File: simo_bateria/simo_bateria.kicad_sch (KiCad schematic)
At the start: 7 parts, among them J1 conector_bateria, J2 conector_bateria, U1 conversor_dc_1_1

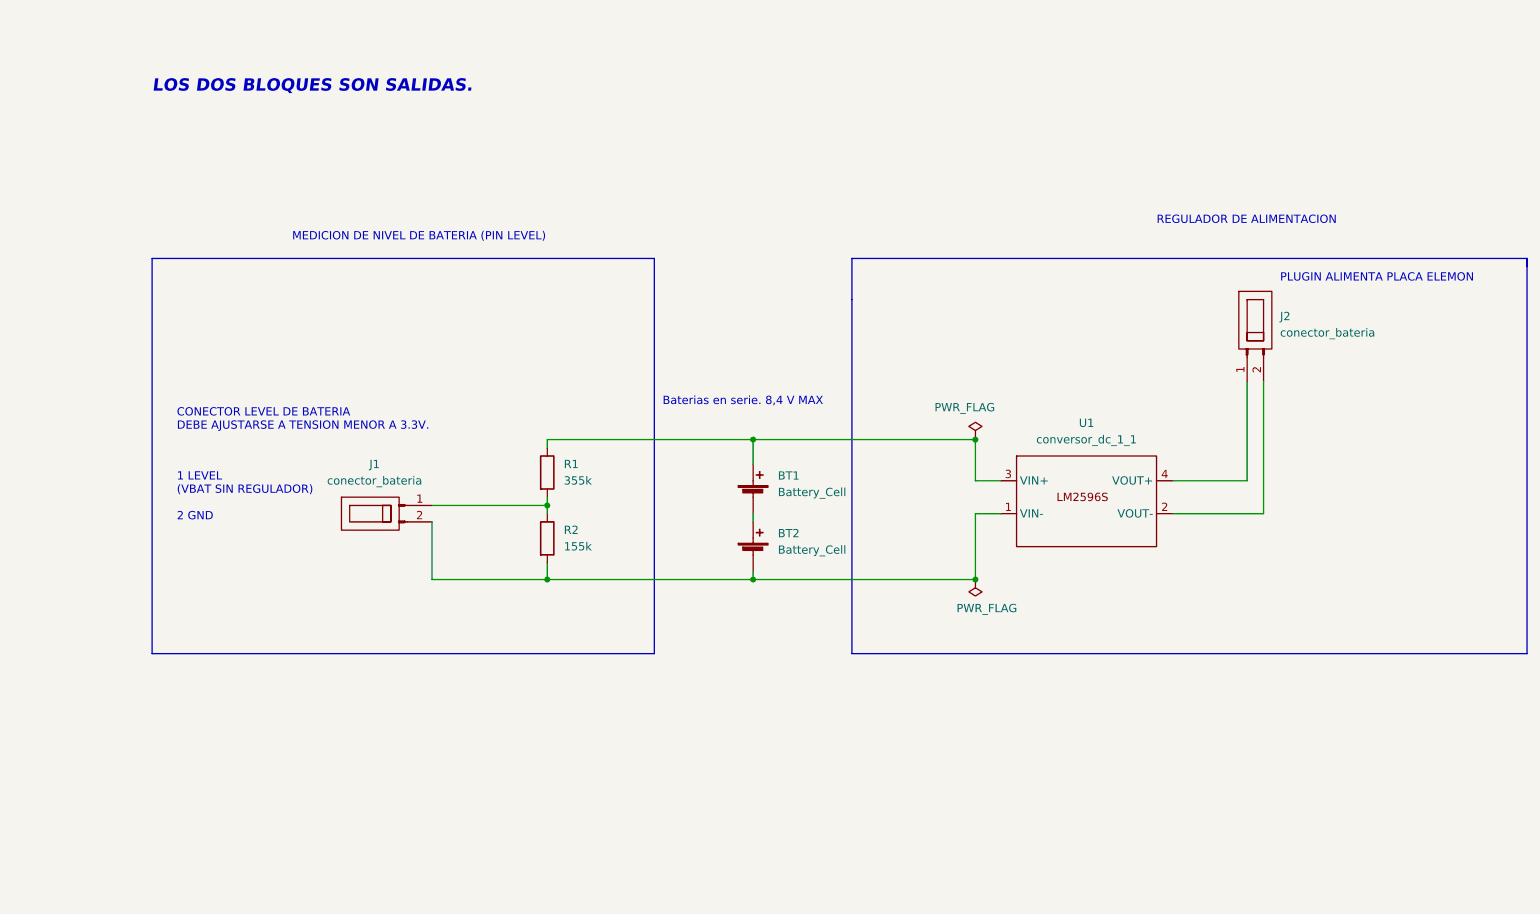
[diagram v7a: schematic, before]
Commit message: update pcb:simo_bateria. Listo para segunda revision
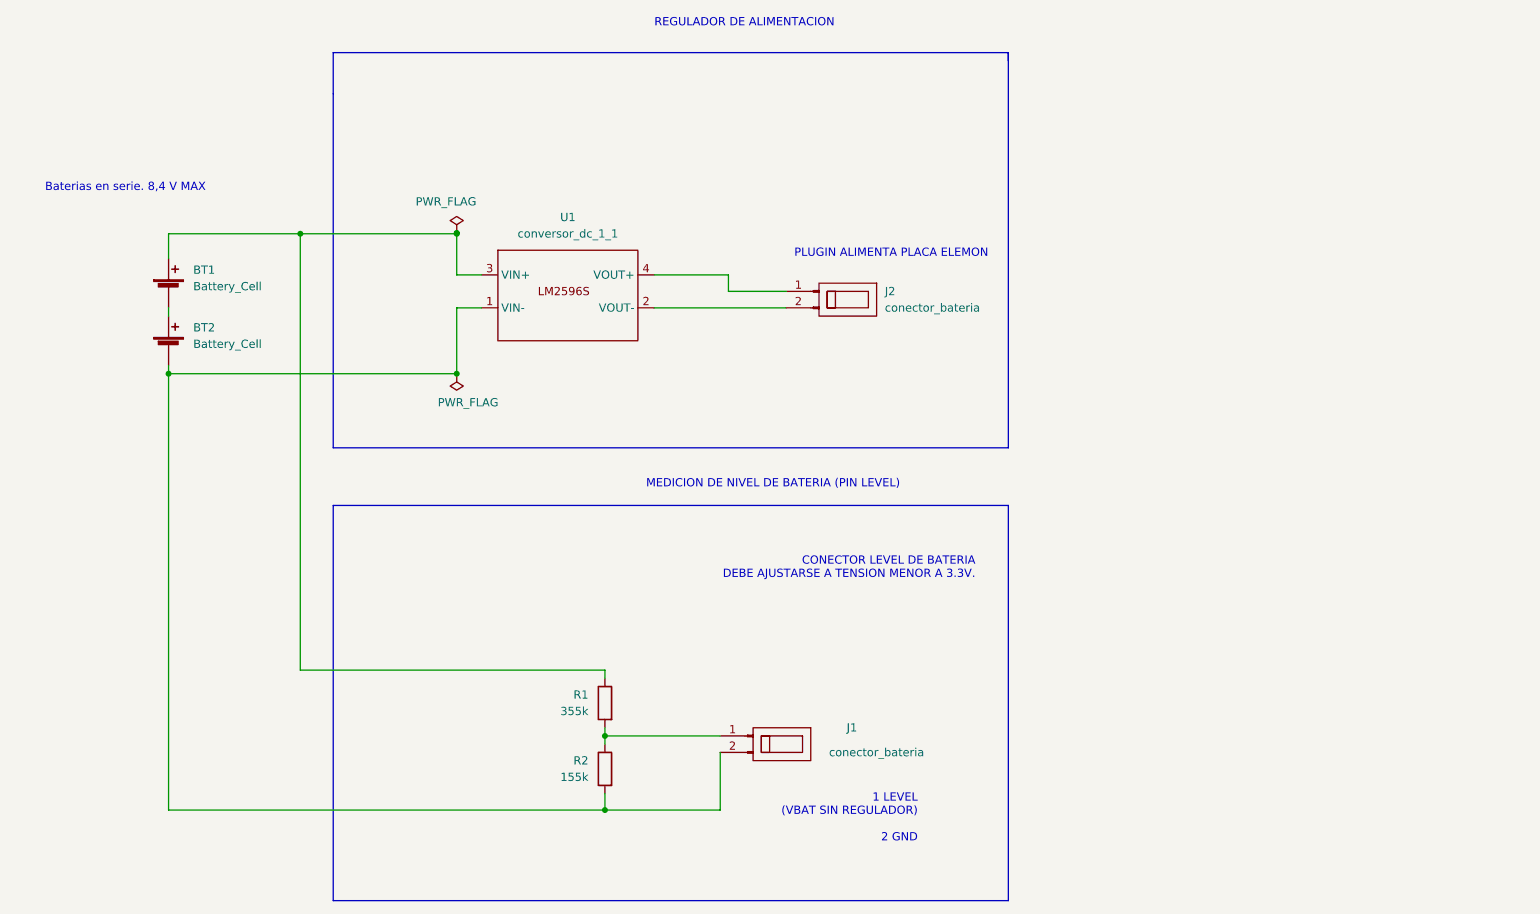
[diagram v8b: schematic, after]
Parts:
- BT1, BT2: Bateria (none) -> https://www.efestpower.com/index.php?ac=article&at=read&did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
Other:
- note removed: "LOS DOS BLOQUES SON SALIDAS."
- moved on the sheet: BT1, BT2, J1, J2, R1, R2, U1
